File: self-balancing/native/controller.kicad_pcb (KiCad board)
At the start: 6 copper layers, 38 x 38 mm, 151 parts, among them J101 G, J102 5V, J103 T1, J104 R1, J105 G, J106 5V, J107 T2, J108 R2, J109 G, J110 5V, J111 T3, J112 R3, J113 G, J114 5V, J115 T4, J116 R4, J117 G, J118 3V3, J119 SCL, J120 SDA, J121 INT, J122 G, J123 G, J124 3V3, J125 SCK, J126 MISO, J127 MOSI, J128 CS, J129 G, J130 3V3, J131 CAN_RX, J132 CAN_TX, J133 G, J134 OUT1, J135 OUT2, J136 OUT3, J137 OUT4, J138 G, J139 OUT5, J140 OUT6, J141 OUT7, J142 OUT8, J143 G_LINK, J144 5V_LINK, J145 LINK_TX, J146 LINK_RX, J147 RUN, J148 M_OK, J149 G, J150 VTREF, J151 SWDIO, J152 SWCLK, J153 NRST, J154 BOOT, J155 G, J156 3V3, J157 ADC1, J158 ADC2, J159 ADC3, J160 RPM, J161 G, J162 3V3, J163 LED, J164 BUZ, J165 PC8, J166 PC9, J167 PD14, J2 TYPE-C-31-M-12, J3 MOTOR / 6-wire, J4 EXT SPI SENSOR, J5 GPS / UART4, Q1 2N7002, Q2 DMN2310UW-7, U1 STM32H743VIT6, U10 SN74LVC2G17DBVR, U11 W25N01GVZEIG / 128MiB, U12 TLV803EA29DBZR, U13 TPS2116DRLR, U2 TPS62162DSGR / 3.3V, U3 ICM-42688-P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

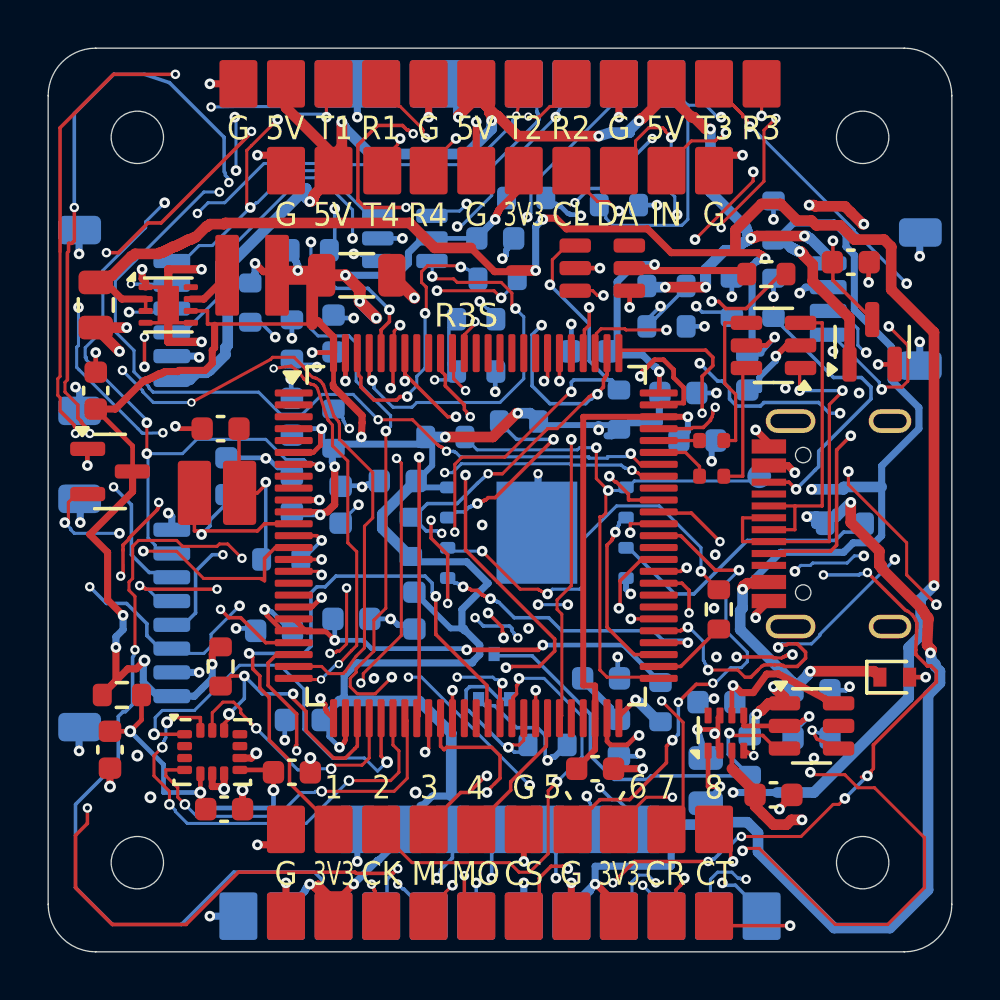
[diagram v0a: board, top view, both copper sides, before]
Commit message: improved routing by removing small segments
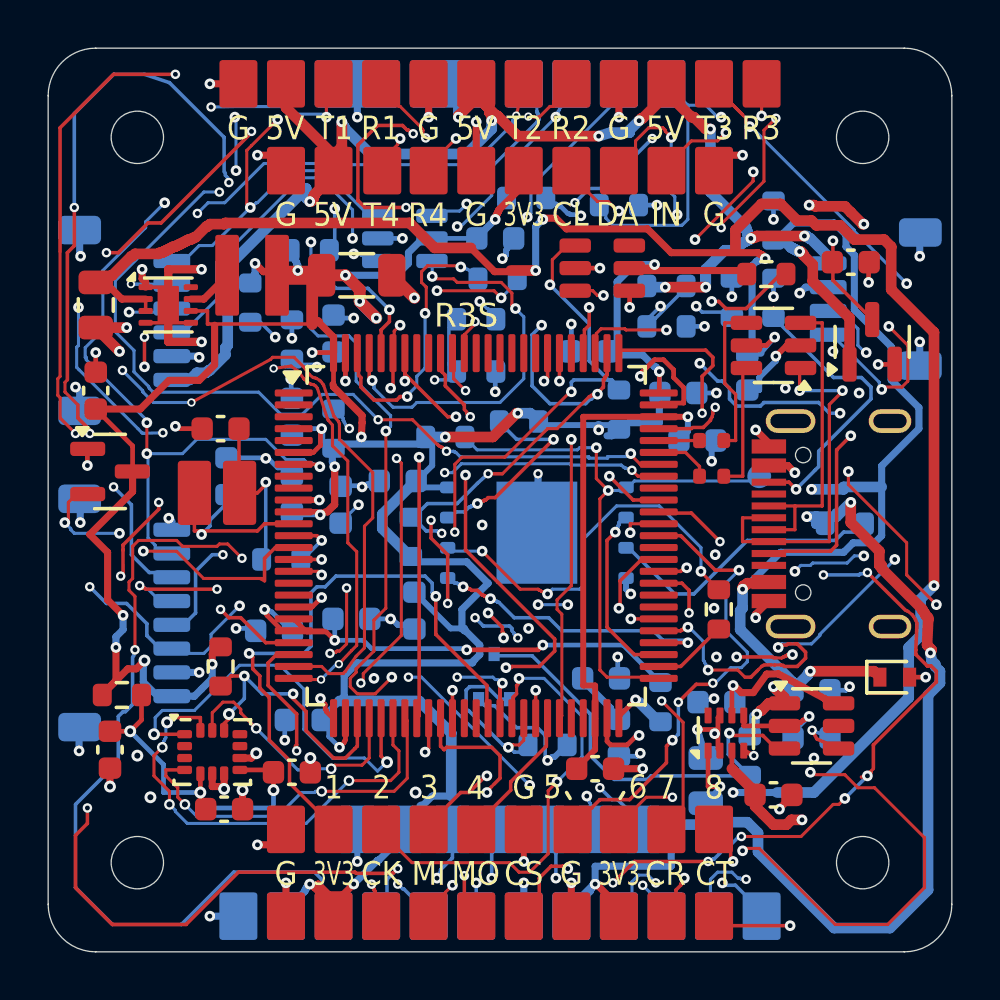
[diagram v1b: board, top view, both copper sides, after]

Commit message: merged small segments
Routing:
- net HOST_RUN_LINK: track 29.6 -> 31.4 mm
- net NRST: track 81.4 -> 80.2 mm
- net VDDA: track 22.1 -> 21.0 mm
- net UART2_TX: track 52.1 -> 51.4 mm

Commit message: merged small segments
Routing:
- net SWCLK: track 52.2 -> 54.3 mm
- net VCAP: track 21.2 -> 20.5 mm

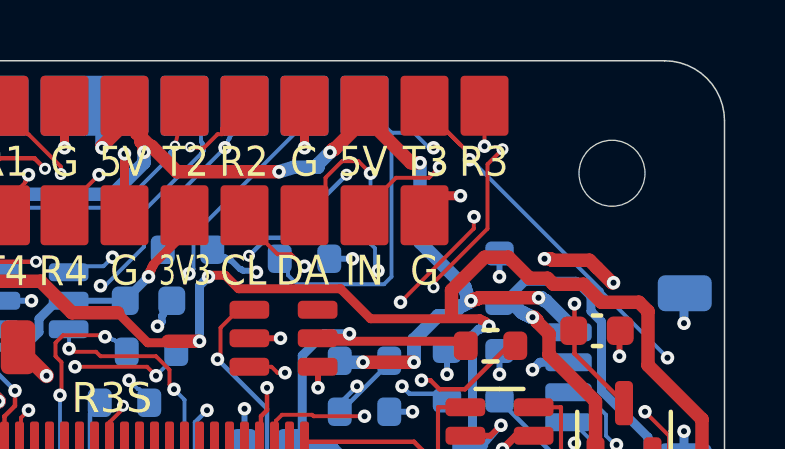
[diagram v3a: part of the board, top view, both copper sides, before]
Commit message: Fix controller zone fill and native DRC metadata
Refill GND zones after b3a2708 routing edits, remove a copper-neutral redundant UART3_TX segment, and align blank LCSC fields with the schematic. Exact checked PCB SHA256: 1fb4bc1b480e8cfed90fecf4bd843177304ffb22e908799fb2268919e2f8912a. KiCad 10.0.6 DRC/ERC/connectivity/parity all clean.
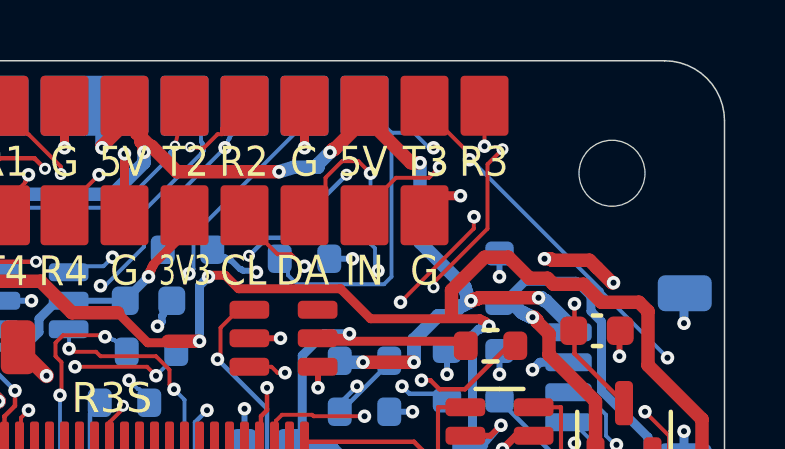
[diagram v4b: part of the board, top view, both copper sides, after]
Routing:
- net UART3_TX: track 41.7 -> 40.7 mm

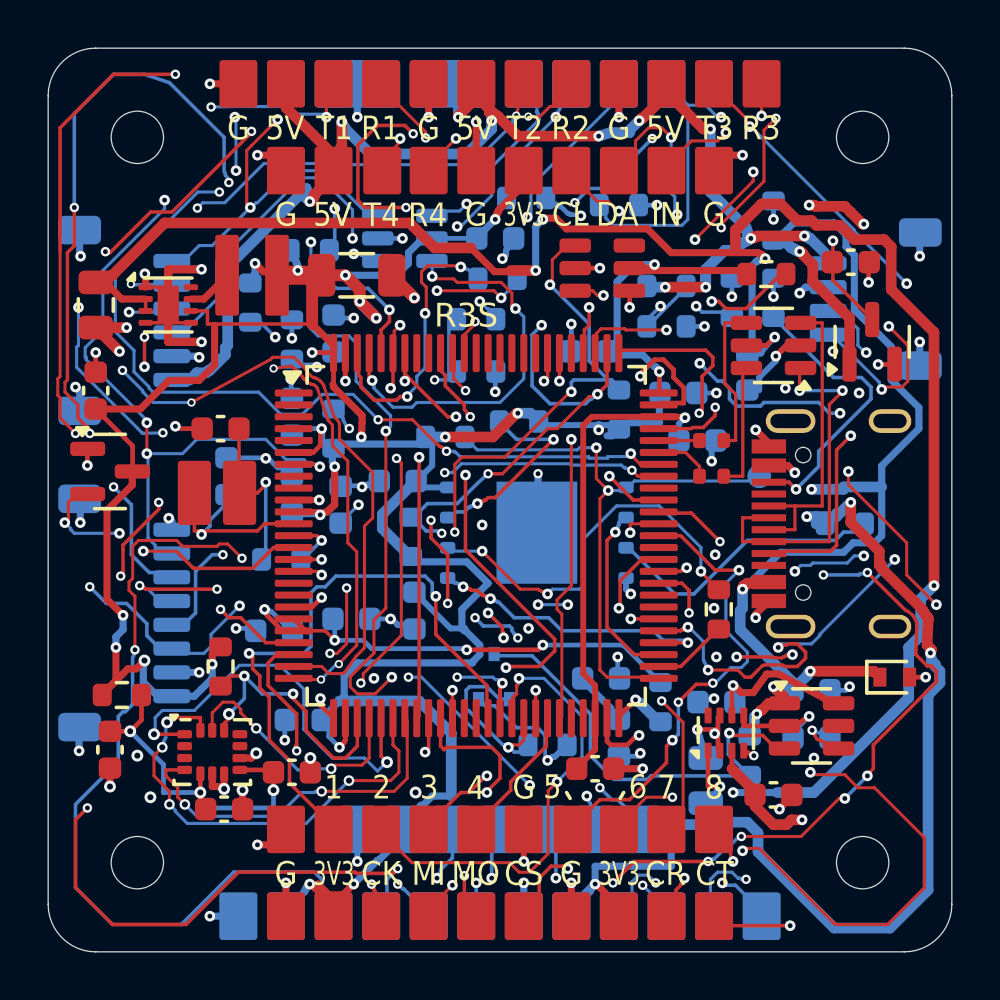
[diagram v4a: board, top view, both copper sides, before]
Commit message: added library and differential rules
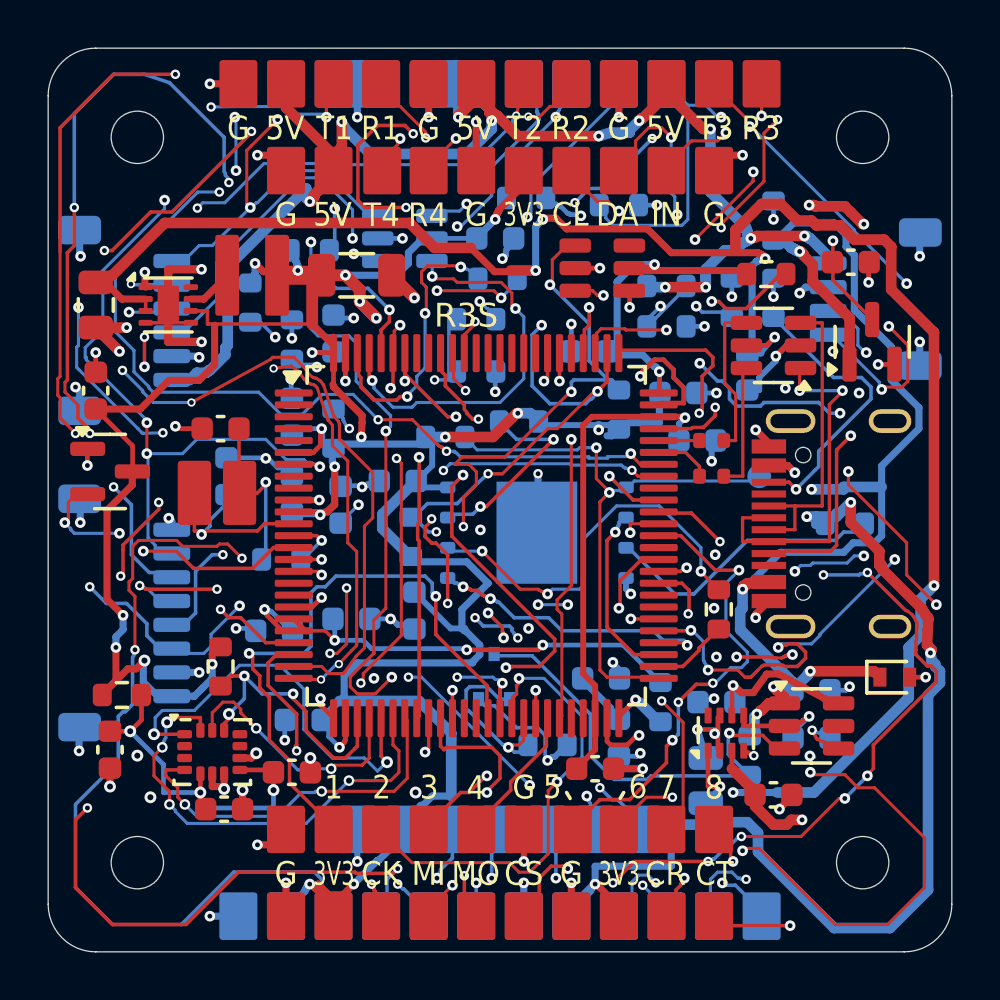
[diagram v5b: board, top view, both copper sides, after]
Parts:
- C1: footprint Capacitor_SMD:C_0805_2012Metric -> H743_Board:C1_C_0805_2012Metric
- C10: footprint Capacitor_SMD:C_0603_1608Metric -> H743_Board:C10_C_0603_1608Metric
- C11: footprint Capacitor_SMD:C_0603_1608Metric -> H743_Board:C11_C_0603_1608Metric
- C12: footprint Capacitor_SMD:C_0603_1608Metric -> H743_Board:C12_C_0603_1608Metric
- C13: footprint Capacitor_SMD:C_0603_1608Metric -> H743_Board:C13_C_0603_1608Metric
- C14: footprint Capacitor_SMD:C_0603_1608Metric -> H743_Board:C14_C_0603_1608Metric
- C15: footprint Capacitor_SMD:C_0603_1608Metric -> H743_Board:C15_C_0603_1608Metric
- C16: footprint Capacitor_SMD:C_0603_1608Metric -> H743_Board:C16_C_0603_1608Metric
- C2: footprint Capacitor_SMD:C_1206_3216Metric -> H743_Board:C2_C_1206_3216Metric
- C24: footprint Capacitor_SMD:C_0603_1608Metric -> H743_Board:C24_C_0603_1608Metric
- C25: footprint Capacitor_SMD:C_0603_1608Metric -> H743_Board:C25_C_0603_1608Metric
- C26: footprint Capacitor_SMD:C_0603_1608Metric -> H743_Board:C26_C_0603_1608Metric
- C29: footprint Capacitor_SMD:C_0603_1608Metric -> H743_Board:C29_C_0603_1608Metric
- C3: footprint Capacitor_SMD:C_0603_1608Metric -> H743_Board:C3_C_0603_1608Metric
- C31: footprint Capacitor_SMD:C_0603_1608Metric -> H743_Board:C31_C_0603_1608Metric
- C32: footprint Capacitor_SMD:C_0603_1608Metric -> H743_Board:C32_C_0603_1608Metric
- C33: footprint Capacitor_SMD:C_0603_1608Metric -> H743_Board:C33_C_0603_1608Metric
- C34: footprint Capacitor_SMD:C_0603_1608Metric -> H743_Board:C34_C_0603_1608Metric
- C35: footprint Capacitor_SMD:C_0603_1608Metric -> H743_Board:C35_C_0603_1608Metric
- C36: footprint Capacitor_SMD:C_0603_1608Metric -> H743_Board:C36_C_0603_1608Metric
- C37: footprint Capacitor_SMD:C_0603_1608Metric -> H743_Board:C37_C_0603_1608Metric
- C38: footprint Capacitor_SMD:C_0603_1608Metric -> H743_Board:C38_C_0603_1608Metric
- C39: footprint Capacitor_SMD:C_0603_1608Metric -> H743_Board:C39_C_0603_1608Metric
- C4: footprint Capacitor_SMD:C_0603_1608Metric -> H743_Board:C4_C_0603_1608Metric
- C40: footprint Capacitor_SMD:C_0603_1608Metric -> H743_Board:C40_C_0603_1608Metric
- C41: footprint Capacitor_SMD:C_0805_2012Metric -> H743_Board:C41_C_0805_2012Metric
- C5: footprint Capacitor_SMD:C_0603_1608Metric -> H743_Board:C5_C_0603_1608Metric
- C6: footprint Capacitor_SMD:C_0603_1608Metric -> H743_Board:C6_C_0603_1608Metric
- C7: footprint Capacitor_SMD:C_0603_1608Metric -> H743_Board:C7_C_0603_1608Metric
- C8: footprint Capacitor_SMD:C_0603_1608Metric -> H743_Board:C8_C_0603_1608Metric
- C9: footprint Capacitor_SMD:C_0603_1608Metric -> H743_Board:C9_C_0603_1608Metric
- J4: footprint Connector_JST:JST_SH_SM08B-SRSS-TB_1x08-1MP_P1.00mm_Horizontal -> H743_Board:J4_JST_SH_SM08B-SRSS-TB_1x08-1MP_P1.00mm_Horizontal
- J5: footprint Connector_JST:JST_SH_SM04B-SRSS-TB_1x04-1MP_P1.00mm_Horizontal -> H743_Board:J5_JST_SH_SM04B-SRSS-TB_1x04-1MP_P1.00mm_Horizontal
- Q1: footprint Package_TO_SOT_SMD:SOT-23 -> H743_Board:Q1_SOT-23
- R1: footprint Resistor_SMD:R_0603_1608Metric -> H743_Board:R1_R_0603_1608Metric
- R10: footprint Resistor_SMD:R_0603_1608Metric -> H743_Board:R10_R_0603_1608Metric
- R11: footprint Resistor_SMD:R_0603_1608Metric -> H743_Board:R11_R_0603_1608Metric
- R12: footprint Resistor_SMD:R_0603_1608Metric -> H743_Board:R12_R_0603_1608Metric
- R13: footprint Resistor_SMD:R_0603_1608Metric -> H743_Board:R13_R_0603_1608Metric
- R2: footprint Resistor_SMD:R_0603_1608Metric -> H743_Board:R2_R_0603_1608Metric
- R3: footprint Resistor_SMD:R_0603_1608Metric -> H743_Board:R3_R_0603_1608Metric
- R4: footprint Resistor_SMD:R_0603_1608Metric -> H743_Board:R4_R_0603_1608Metric
- R42: footprint Resistor_SMD:R_0603_1608Metric -> H743_Board:R42_R_0603_1608Metric
- R43: footprint Resistor_SMD:R_0603_1608Metric -> H743_Board:R43_R_0603_1608Metric
- R44: footprint Resistor_SMD:R_0603_1608Metric -> H743_Board:R44_R_0603_1608Metric
- R45: footprint Resistor_SMD:R_0603_1608Metric -> H743_Board:R45_R_0603_1608Metric
- R46: footprint Resistor_SMD:R_0603_1608Metric -> H743_Board:R46_R_0603_1608Metric
- R48: footprint Resistor_SMD:R_0603_1608Metric -> H743_Board:R48_R_0603_1608Metric
- R49: footprint Resistor_SMD:R_0603_1608Metric -> H743_Board:R49_R_0603_1608Metric
- R5: footprint Resistor_SMD:R_0603_1608Metric -> H743_Board:R5_R_0603_1608Metric
- R50: footprint Resistor_SMD:R_0603_1608Metric -> H743_Board:R50_R_0603_1608Metric
- R51: footprint Resistor_SMD:R_0603_1608Metric -> H743_Board:R51_R_0603_1608Metric
- R52: footprint Resistor_SMD:R_0603_1608Metric -> H743_Board:R52_R_0603_1608Metric
- R53: footprint Resistor_SMD:R_0603_1608Metric -> H743_Board:R53_R_0603_1608Metric
- R54: footprint Resistor_SMD:R_0603_1608Metric -> H743_Board:R54_R_0603_1608Metric
- R55: footprint Resistor_SMD:R_0603_1608Metric -> H743_Board:R55_R_0603_1608Metric
- R56: footprint Resistor_SMD:R_0603_1608Metric -> H743_Board:R56_R_0603_1608Metric
- R57: footprint Resistor_SMD:R_0603_1608Metric -> H743_Board:R57_R_0603_1608Metric
- R58: footprint Resistor_SMD:R_0603_1608Metric -> H743_Board:R58_R_0603_1608Metric
- R6: footprint Resistor_SMD:R_0603_1608Metric -> H743_Board:R6_R_0603_1608Metric
- R9: footprint Resistor_SMD:R_0603_1608Metric -> H743_Board:R9_R_0603_1608Metric
- U1: footprint Package_QFP:LQFP-100_14x14mm_P0.5mm -> H743_Board:U1_LQFP-100_14x14mm_P0.5mm
- U10: footprint Package_TO_SOT_SMD:SOT-23-6 -> H743_Board:U10_SOT-23-6
- U11: footprint Package_SON:WSON-8-1EP_8x6mm_P1.27mm_EP3.4x4.3mm -> H743_Board:U11_WSON-8-1EP_8x6mm_P1.27mm_EP3.4x4.3mm
- U12: footprint Package_TO_SOT_SMD:SOT-23 -> H743_Board:U12_SOT-23
- U13: footprint Package_TO_SOT_SMD:SOT-583-8 -> H743_Board:U13_SOT-583-8
- U3: footprint Package_LGA:LGA-14_3x2.5mm_P0.5mm_LayoutBorder3x4y -> H743_Board:U3_LGA-14_3x2.5mm_P0.5mm_LayoutBorder3x4y
- U4: footprint Package_TO_SOT_SMD:SOT-23-6 -> H743_Board:U4_SOT-23-6
- U6: footprint Package_TO_SOT_SMD:SOT-23-6 -> H743_Board:U6_SOT-23-6
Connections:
- net /power/USB_DM_CONN renamed /power/USB_CONN_N
- net /power/USB_DM_ESD renamed /power/USB_ESD_N
- net /power/USB_DP_CONN renamed /power/USB_CONN_P
- net /power/USB_DP_ESD renamed /power/USB_ESD_P
- net USB_DM_MCU renamed USB_MCU_N
- net USB_DP_MCU renamed USB_MCU_P
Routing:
- net SWCLK: track 54.3 -> 52.9 mm
- net FDCAN1_RX: track 39.7 -> 38.5 mm
- net MOTOR_TX_LINK: track 33.5 -> 32.7 mm
